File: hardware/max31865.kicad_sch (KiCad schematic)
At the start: 20 parts, among them U2 MIC5225-3.3YM5-TR, U3 MAX31865xAP

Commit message: initial commit, complete schematic and board
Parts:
- removed C5, C6: 10u, symbol Device:C
- removed D2, D3, D4: 1N4148, Diode_THT:D_DO-35_SOD27_P7.62mm_Horizontal, symbol Diode:1N4148
- removed JP1: SJ2C, symbol Jumper:SolderJumper_2_Bridged
- removed R1, R2, R3: 10k, symbol Device:R
- removed U2: MIC5225-3.3YM5-TR, Package_TO_SOT_SMD:SOT-23-5, symbol Regulator_Linear:MIC5205YM5
- C5: renamed from C7; footprint (none) -> Capacitor_SMD:C_0805_2012Metric_Pad1.18x1.45mm_HandSolder
- C6: renamed from C8; footprint (none) -> Capacitor_SMD:C_0805_2012Metric_Pad1.18x1.45mm_HandSolder
- Cl1: footprint (none) -> Capacitor_SMD:C_0805_2012Metric_Pad1.18x1.45mm_HandSolder
- FB1, Rref1: footprint (none) -> Resistor_SMD:R_0805_2012Metric_Pad1.20x1.40mm_HandSolder
- JP1: renamed from JP2; footprint (none) -> Jumper:SolderJumper-2_P1.3mm_Open_TrianglePad1.0x1.5mm
- JP2: renamed from JP3; footprint (none) -> Jumper:SolderJumper-2_P1.3mm_Bridged_RoundedPad1.0x1.5mm
- JP3: renamed from JP4; footprint (none) -> Jumper:SolderJumper-2_P1.3mm_Open_TrianglePad1.0x1.5mm
- JP4: renamed from JP5; footprint (none) -> Jumper:SolderJumper-2_P1.3mm_Open_TrianglePad1.0x1.5mm
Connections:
- net SDO: no longer U3.1 (~{DRDY})
- net SCLK: now reaches U3.15 (SCLK)
- net CS: now reaches U3.16 (~{CS})
- net SDI: now reaches U3.14 (SDI)
- new net DRDY: U3.1 (~{DRDY})
- no-connect marks 1 -> 0
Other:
- note removed: "cut jumper if supplying 3V3 or DNP this circuit"

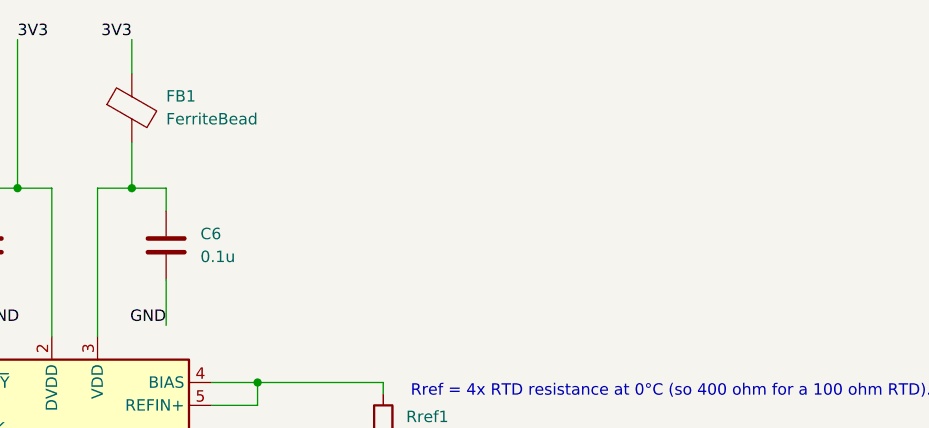
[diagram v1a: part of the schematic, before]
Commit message: review and revise board to use kmlib properly and clear drc/erc
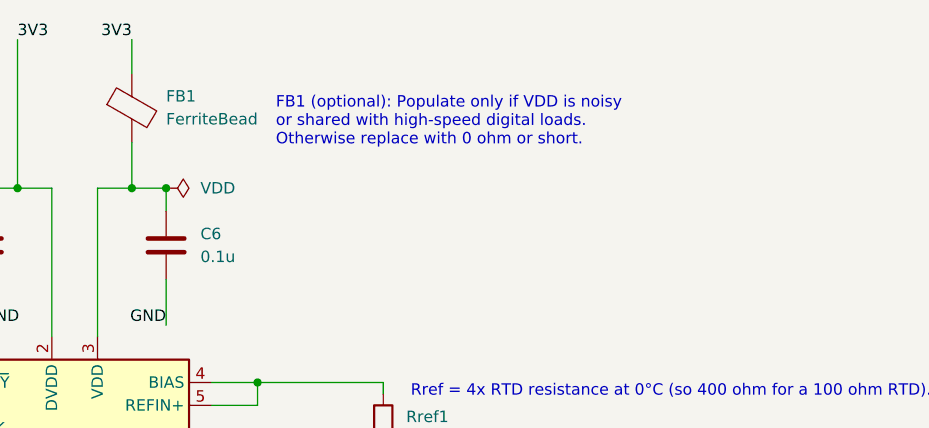
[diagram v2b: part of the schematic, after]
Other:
- note added: "FB1 (optional): Populate only if VDD is noisy or shared with high-speed digital loads. Otherwise replace with 0 ohm or short."
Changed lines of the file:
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@@
 	(generator_version "9.0")
 	(paper "A4")
+	(text "FB1 (optional): Populate only if VDD is noisy \nor shared with high-speed digital loads.\nOtherwise replace with 0 ohm or short."
+		(exclude_from_sim no)
+		(at 156.972 53.594 0)
+		(effects
+			(font
+				(size 1.27 1.27)
+			)
+			(justify left)
+		)
+	)
 	(text "4 wire: \n	- config: JUMP1 OPEN, JUMP2 CLOSED, JUMP3 OPEN, JUMP4 OPEN\n	- changes from prod: none (default)\n3 wire: \n	- config: JUMP1 CLOSED, JUMP2 OPEN, JUMP3 OPEN, JUMP4 OPEN\n	- changes from prod: solder short JUMP1 closed and cut JUMP2\n2 wire: \n	- config: JUMP1 OPEN, JUMP2 CLOSED, JUMP3 CLOSED, JUMP4 CLOSED\n	- changes from prod: solder short JUMP3 & JUMP4 closed\n"
 		(exclude_from_sim no)
@@
 	(junction
 		(at 128.27 60.96)
+		(diameter 0)
+		(color 0 0 0 0)
+	)
+	(junction
+		(at 144.78 60.96)
 		(diameter 0)
 		(color 0 0 0 0)
@@
 					(unit 1)
 				)
+			)
+		)
+	)
+	(symbol
+		(lib_id "power:PWR_FLAG")
+		(at 144.78 60.96 270)
+		(unit 1)
+		(exclude_from_sim no)
+		(in_bom yes)
+		(on_board yes)
+		(dnp no)
+		(fields_autoplaced yes)
+		(property "Reference" "#FLG04"
+			(at 146.685 60.96 0)
+			(effects
+				(font
+					(size 1.27 1.27)
+				)
+				(hide yes)
+			)
+		)
+		(property "Value" "VDD"
+			(at 148.59 60.9599 90)
+			(effects
+				(font
+					(size 1.27 1.27)
+				)
+				(justify left)
+			)
+		)
+		(property "Footprint" ""
+			(at 144.78 60.96 0)
+			(effects
+				(font
+					(size 1.27 1.27)
+				)
+				(hide yes)
+			)
+		)
+		(property "Datasheet" "~"
+			(at 144.78 60.96 0)
+			(effects
+				(font
+					(size 1.27 1.27)
+				)
+				(hide yes)
+			)
+		)
+		(property "Description" "Special symbol for telling ERC where power comes from"
+			(at 144.78 60.96 0)
+			(effects
+				(font
+					(size 1.27 1.27)
+				)
+				(hide yes)
+			)
+		)
+		(pin "1"
+		)
+		(instances
+			(project ""
+				(path "/66043bca-a260-4915-9fce-8a51d324c687/8d443f08-44e3-4cb8-98b2-f920fc9e6b8c"
+					(reference "#FLG04")
+					(unit 1)
+				)
+				(path "/66043bca-a260-4915-9fce-8a51d324c687/91f3c1da-7e16-4cfd-984a-eae65aa817f4"
+					(reference "#FLG07")
+					(unit 1)
+				)
+				(path "/66043bca-a260-4915-9fce-8a51d324c687/c1e0fb7d-e3e2-40a1-99cb-0ef960c71346"
+					(reference "#FLG06")
+					(unit 1)
+				)
+				(path "/66043bca-a260-4915-9fce-8a51d324c687/fab02d98-7a25-457b-aaf2-ee11c9a5ed50"
+					(reference "#FLG05")
+					(unit 1)
+				)
